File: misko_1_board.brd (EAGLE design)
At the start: 115 x 115 mm, 152 parts, among them IC1 ATMEGA1281-16AU, IC10 ORG1510-MK4, IC11 TPS3808G33DBVT, IC12 LTC4425, IC13 RN4678_BT_MODULE, IC14 ADXL345, IC15 74HCT1G32, IC16 FM25W256-SOIC, IC17 MICROSD_SPI_MODE, IC18 FH12-30S-0.5SH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

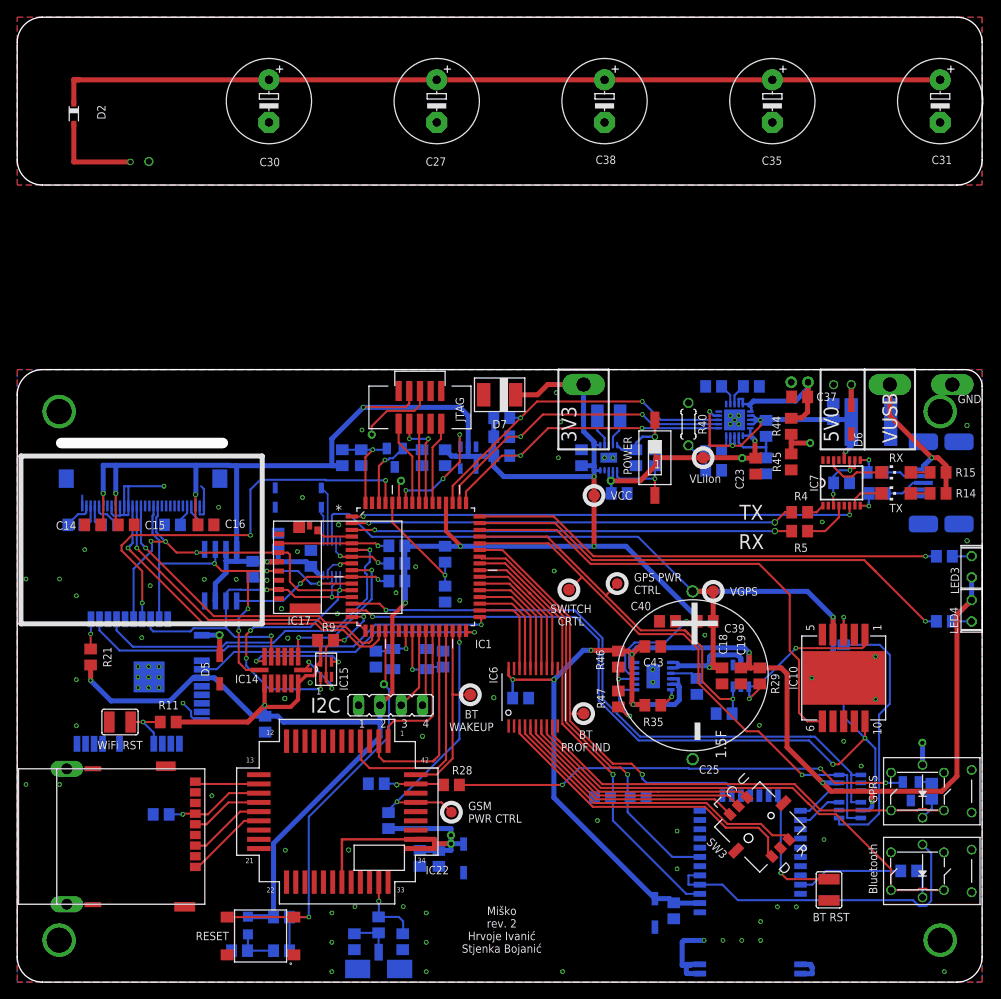
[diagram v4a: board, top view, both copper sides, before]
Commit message: - aligned tplace/bplace stuff to grid
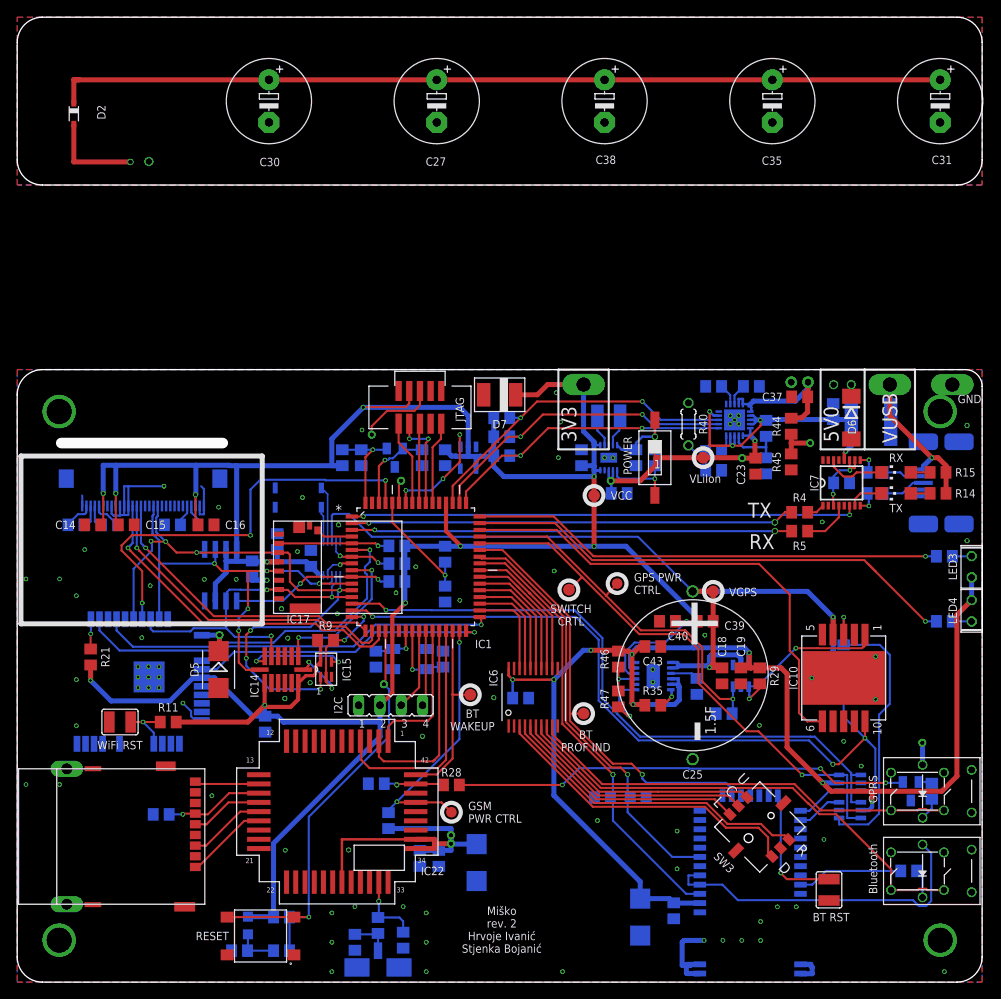
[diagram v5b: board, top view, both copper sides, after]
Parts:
- D3: value BZT52C5V1-E3-18 -> SZ1SMB5916BT3G; device zener:SOD123 -> diode:SMB
- D4: value BZT52C3V3-E3-08 -> SZ1SMB5916BT3G; device zener:SOD123 -> diode:SMB
- D5: value BZT52C4V3-E3-18 -> SZ1SMB5916BT3G; device zener:SOD123 -> diode:SMB
- D6: value 1N4733AW-TP -> SMBJ5339B-TP; device zener:SOD123 -> diode:DO214AA
- moved D4 1.82 mm to (74.2, 7.75)
- moved D3 1.63 mm to (54.8, 14.2)
- moved D6 0.25 mm to (99.4, 67.3)
- moved R6 0.25 mm to (102.2, 58.2)
- moved CONN5 0.20 mm to (43.0, 1.75)
- moved C28 0.19 mm to (46.0, 5.00)
- moved D5 0.13 mm to (24.0, 37.2)
- moved C36 0.11 mm to (31.0, 52.5)
- moved R38 0.10 mm to (43.0, 6.75)
- moved C33 0.09 mm to (40.2, 4.75)
- moved C21 0.07 mm to (28.0, 49.2)
- moved IC14 0.05 mm to (31.5, 37.2)
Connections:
- net 5V0: now also D6.C; no longer D6.CAT
- net GND: now also D3.A, D4.A, D5.A, D6.A; no longer D3.AN, D4.AN, D5.AN, D6.AN
- net VCC: now also D4.C; no longer D4.CAT
- net V_LIION+: now also D3.C, D5.C; no longer D3.CAT, D5.CAT
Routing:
- net 5V0: track 53.2 -> 51.8 mm
- net V_LIION+: track 59.3 -> 60.4 mm
- net VCC: track 516.7 -> 517.8 mm
